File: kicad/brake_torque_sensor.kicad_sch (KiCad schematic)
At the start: 6 parts, among them J901 Conn_Coaxial_HL-BNC-KHDA

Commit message: Update brake design block and remove torque block
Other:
- removed sheet torque_bridge_0_3v3_ina821
- sheet brake_current_sink_0_49ma_dac80501 ports: added ~{BRAKE_FAULT}_INST; removed none
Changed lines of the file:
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@@
+		)
+	)
+	(wire
+		(pts
+			(xy 106.68 96.52) (xy 109.22 96.52)
+		)
+		(stroke
+			(width 0)
+			(type default)
 		)
 	)
@@
 		(shape output)
 		(at 205.74 81.28 0)
+		(effects
+			(font
+				(size 1.27 1.27)
+			)
+			(justify left)
+		)
+	)
+	(hierarchical_label "~{BRAKE_FAULT}_INST"
+		(shape output)
+		(at 109.22 96.52 0)
 		(effects
 			(font
@@
 	(group "brake_current_sink_0_49ma_dac80501"
 		(lib_id "orb_weaver_private:brake_current_sink_0_49ma_dac80501")
-		(members "6e3dbbf0-8149-4c85-8221-1ff1f94a4cf2")
-	)
-	(group "torque_bridge_0_3v3_ina821"
-		(lib_id "orb_weaver_private:torque_bridge_0_3v3_ina821")
-		(members "37b34092-76aa-4332-ba5e-f593ea9d6ee8")
+		(members "b54345b5-7b7e-4363-9fd3-934646b4d877")
 	)
 	(group "hv_to_12v_tpsm365r6"
 		(lib_id "orb_weaver_private:hv_to_12v_tpsm365r6")
 		(members "670aba7c-5d0b-40f5-98be-71b6a2ad93fc")
-	)
-	(sheet
-		(at 177.8 76.2)
-		(size 25.4 33.02)
-		(exclude_from_sim no)
-		(in_bom yes)
-		(on_board yes)
-		(dnp no)
-		(fields_autoplaced yes)
-		(stroke
-			(width 0.1524)
-			(type solid)
-		)
-		(fill
-			(color 0 0 0 0)
-		)
-		(property "Sheetname" "torque_bridge_0_3v3_ina821"
-			(at 177.8 75.4884 0)
-			(show_name no)
-			(do_not_autoplace no)
-			(effects
-				(font
-					(size 1.27 1.27)
-				)
-				(justify left bottom)
-			)
-		)
-		(property "Sheetfile" "torque_bridge_0_3v3_ina821.kicad_sch"
-			(at 177.8 109.8046 0)
-			(show_name no)
-			(do_not_autoplace no)
-			(effects
-				(font
-					(size 1.27 1.27)
-				)
-				(justify left top)
-			)
-		)
-		(pin "+3.3V" passive
-			(at 177.8 83.82 180)
-			(effects
-				(font
-					(size 1.27 1.27)
-				)
-				(justify left)
-			)
-		)
-		(pin "+5V" passive
-			(at 177.8 81.28 180)
-			(effects
-				(font
-					(size 1.27 1.27)
-				)
-				(justify left)
-			)
-		)
-		(pin "+12V" passive
-			(at 177.8 78.74 180)
-			(effects
-				(font
-					(size 1.27 1.27)
-				)
-				(justify left)
-			)
-		)
-		(pin "GND" passive
-			(at 177.8 86.36 180)
-			(effects
-				(font
-					(size 1.27 1.27)
-				)
-				(justify left)
-			)
-		)
-		(pin "SCK" input
-			(at 177.8 93.98 180)
-			(effects
-				(font
-					(size 1.27 1.27)
-				)
-				(justify left)
-			)
-		)
-		(pin "SDI" input
-			(at 177.8 96.52 180)
-			(effects
-				(font
-					(size 1.27 1.27)
-				)
-				(justify left)
-			)
-		)
-		(pin "SDO" output
-			(at 177.8 99.06 180)
-			(effects
-				(font
-					(size 1.27 1.27)
-				)
-				(justify left)
-			)
-		)
-		(pin "TQ_AOUT" output
-			(at 203.2 78.74 0)
-			(effects
-				(font
-					(size 1.27 1.27)
-				)
-				(justify right)
-			)
-		)
-		(pin "TQ_AOUT_MON" output
-			(at 203.2 81.28 0)
-			(effects
-				(font
-					(size 1.27 1.27)
-				)
-				(justify right)
-			)
-		)
-		(pin "TQ_CAL_EN" input
-			(at 177.8 106.68 180)
-			(effects
-				(font
-					(size 1.27 1.27)
-				)
-				(justify left)
-			)
-		)
-		(pin "TQ_CONVST_CS" input
-			(at 177.8 101.6 180)
-			(effects
-				(font
-					(size 1.27 1.27)
-				)
-				(justify left)
-			)
-		)
-		(instances
-			(project "mouse-joystick-pcb"
-				(path "/004d6f75-7365-204a-6f79-737469636b00/f229cd8b-936a-4ad1-8bff-4cac135737f9"
-					(page "20")
-				)
-			)
-		)
 	)
 	(sheet
@@
 	(sheet
 		(at 76.2 76.2)
-		(size 30.48 30.48)
+		(size 30.48 22.86)
 		(exclude_from_sim no)
 		(in_bom yes)
@@
 		)
 		(property "Sheetfile" "brake_current_sink_0_49ma_dac80501.kicad_sch"
-			(at 76.2 107.2646 0)
+			(at 76.2 99.6446 0)
 			(show_name no)
 			(do_not_autoplace no)
@@
 		)
 		(pin "SCL" input
+			(at 76.2 93.98 180)
+			(effects
+				(font
+					(size 1.27 1.27)
+				)
+				(justify left)
+			)
+		)
+		(pin "SDA" bidirectional
 			(at 76.2 96.52 180)
-			(effects
-				(font
-					(size 1.27 1.27)
-				)
-				(justify left)
-			)
-		)
-		(pin "SDA" bidirectional
-			(at 76.2 93.98 180)
 			(effects
 				(font
@@
 			(effects
 				(font
+					(size 1.27 1.27)
+				)
+				(justify right)
+			)
+		)
+		(pin "~{BRAKE_FAULT}_INST" output
+			(at 106.68 96.52 0)
+			(effects
+				(font

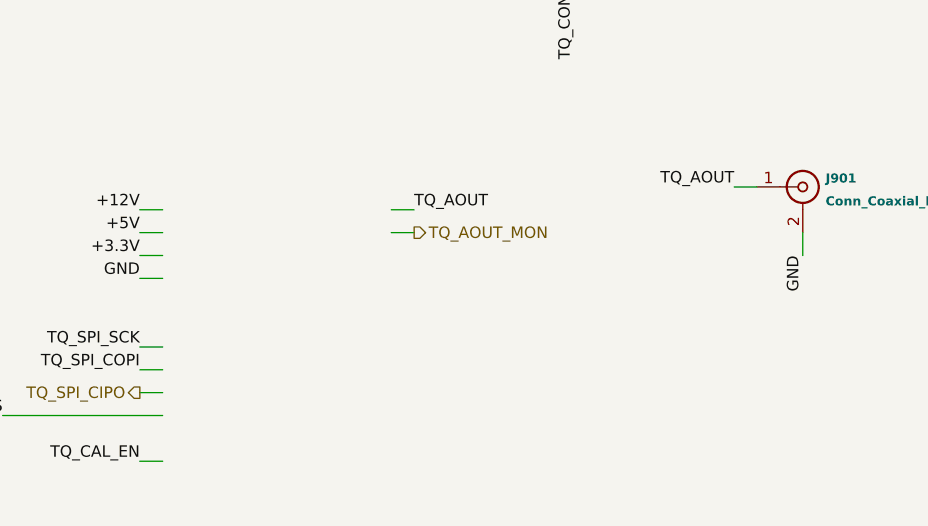
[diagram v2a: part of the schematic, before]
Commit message: Finish v1.0 block replacement for inst resistors
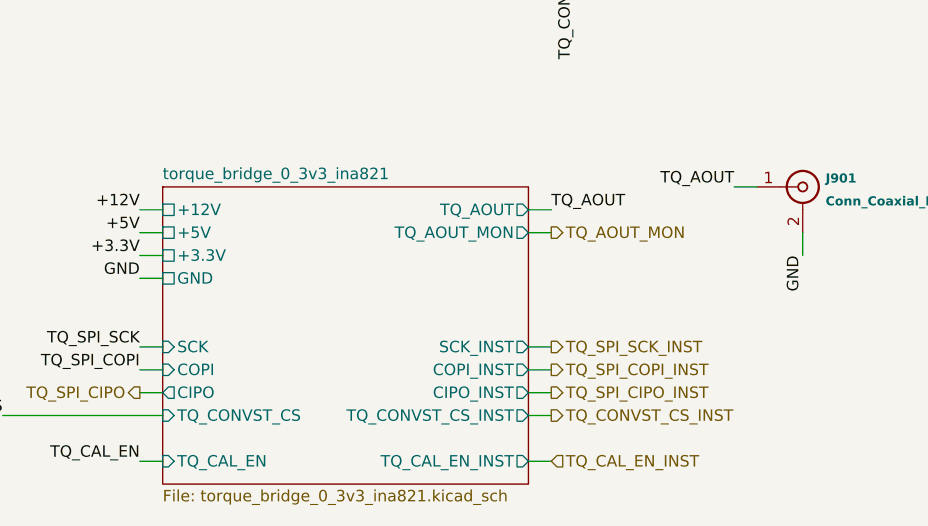
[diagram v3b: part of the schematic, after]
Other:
- added sheet torque_bridge_0_3v3_ina821 (torque_bridge_0_3v3_ina821.kicad_sch)

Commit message: Regenerate schematics
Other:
- sheet hv_to_12v_tpsm365r6 ports: added VOUT; removed +12V
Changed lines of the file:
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@@
 	)
 	(group "hv_to_12v_tpsm365r6"
-		(lib_id "orb_weaver_private:hv_to_12v_tpsm365r6")
+		(lib_id "orb_weaver_tpsm365r6_adjustable:tpsm365r6_adjustable_12v")
 		(members "670aba7c-5d0b-40f5-98be-71b6a2ad93fc")
 	)
@@
 			)
 		)
-		(pin "+12V" passive
+				(pin "VOUT" passive
 			(at 152.4 27.94 0)
 			(effects
